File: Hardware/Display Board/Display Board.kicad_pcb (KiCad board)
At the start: 2 copper layers, 165.1 x 88.9 mm, 44 parts, among them J1 GPS, J10 Conn_02x03_Odd_Even, J11 Conn_02x03_Odd_Even, J12 Conn_02x03_Odd_Even, J13 Conn_02x03_Odd_Even, J14 Conn_02x03_Odd_Even, J15 Conn_02x03_Odd_Even, J16 Conn_02x03_Odd_Even, J17 Conn_02x03_Odd_Even, J18 Conn_02x03_Odd_Even, J19 Conn_02x03_Odd_Even, J2 RTC, J20 Conn_02x03_Odd_Even, J21 Conn_02x03_Odd_Even, J22 Conn_02x03_Odd_Even, J23 Conn_02x03_Odd_Even, J24 Conn_02x03_Odd_Even, J25 Conn_02x03_Odd_Even, J26 Conn_02x03_Odd_Even, J27 Conn_02x03_Odd_Even, J28 Conn_02x03_Odd_Even, J29 Conn_02x03_Odd_Even, J3 CONT, J30 Conn_02x03_Odd_Even, J31 Conn_02x03_Odd_Even, J4 H:M, J5 M:D, J6 M:S, J7 D:Y, J8 Conn_02x03_Odd_Even, J9 Conn_02x03_Odd_Even

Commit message: Components placed
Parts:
- J1, J2, J3: moved to B.Cu
- moved J21 282.3 mm to (77.5, 147.3), turned to -90 degrees
- moved J20 271.6 mm to (72.4, 119.4), turned to 90 degrees
- moved J9 266.6 mm to (77.5, 96.5), turned to -90 degrees
- moved J23 265.7 mm to (100.3, 147.3), turned to -90 degrees
- moved J8 262.1 mm to (72.4, 68.6), turned to 90 degrees
- moved J11 260.1 mm to (100.3, 96.5), turned to -90 degrees
- moved J10 255.5 mm to (95.2, 68.6), turned to 90 degrees
- moved J22 253.3 mm to (95.3, 119.4), turned to 90 degrees
- moved J25 250.2 mm to (130.8, 147.3), turned to -90 degrees
- moved J24 234.5 mm to (125.7, 119.4), turned to 90 degrees
- moved J13 222.8 mm to (130.8, 96.5), turned to -90 degrees
- moved J29 220.0 mm to (184.2, 147.3), turned to -90 degrees
- moved J12 213.3 mm to (125.7, 68.6), turned to 90 degrees
- moved J28 202.2 mm to (179.1, 119.4), turned to 90 degrees
- moved J27 189.6 mm to (153.7, 147.3), turned to -90 degrees
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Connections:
- J1 pad 2: unconnected-(J1-Pin_2-Pad2) -> MCU RX / GPS TX
- J1 pad 3: unconnected-(J1-Pin_3-Pad3) -> MCU TX / GPS RX
- J2 pad 3: unconnected-(J2-Pin_3-Pad3) -> SDA
- J2 pad 4: unconnected-(J2-Pin_4-Pad4) -> SCL
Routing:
- added copper zone on B.Cu, net GND

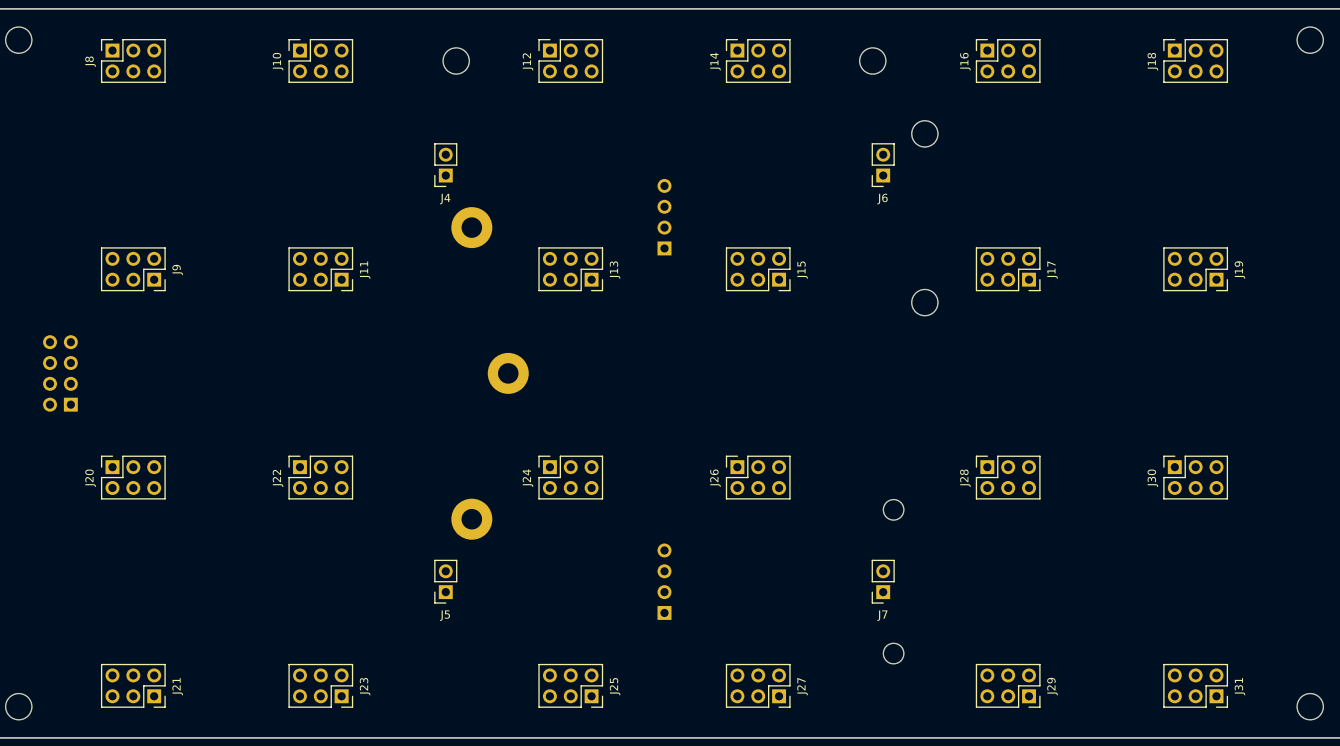
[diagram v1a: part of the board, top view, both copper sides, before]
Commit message: KiCad display board completed
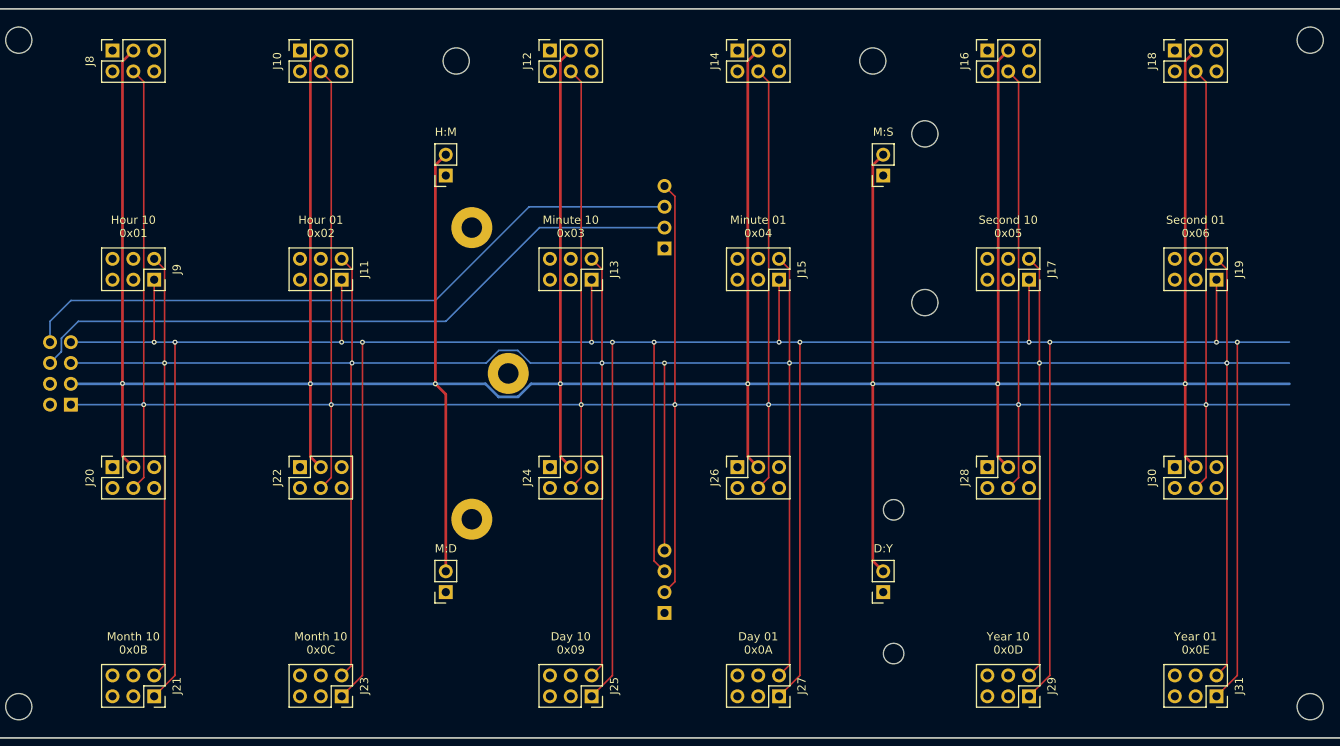
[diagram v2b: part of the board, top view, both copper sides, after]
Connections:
- J21 pad 5: GND -> /Month10/ADDR1
- J23 pad 4: GND -> /Month01/ADDR2
- J23 pad 5: /Month01/ADDR1 -> GND
- J25 pad 5: /Day10/ADDR1 -> GND
- J27 pad 4: /Day01/ADDR2 -> GND
- J27 pad 5: GND -> /Day01/ADDR1
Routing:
- net Vnn: track 0.00 -> 564.9 mm, vias 0 -> 8
- net Vdd: track 0.00 -> 510.3 mm, vias 0 -> 7
- net SDA: track 0.00 -> 488.2 mm, vias 0 -> 13
- net SCL: track 0.00 -> 483.8 mm, vias 0 -> 7
- net MCU TX / GPS RX: track 0.00 -> 83.3 mm
- net MCU RX / GPS TX: track 0.00 -> 82.7 mm
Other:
- board text added: "Day 01 0x0A"
- board text added: "Day 10 0x09"
- board text added: "Hour 01 0x02"
- board text added: "Hour 10 0x01"
- board text added: "Minute 01 0x04"
- board text added: "Minute 10 0x03"
- board text added: "Month 10 0x0B"
- board text added: "Month 10 0x0C"
- board text added: "Second 01 0x06"
- board text added: "Second 10 0x05"
- board text added: "Year 01 0x0E"
- board text added: "Year 10 0x0D"

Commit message: Forgot to save again. (╯°□°）╯︵ ┻━┻
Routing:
- net Vnn: track 564.9 -> 552.2 mm
- net Vdd: track 510.3 -> 500.1 mm
- net SCL: track 483.8 -> 476.2 mm
- net SDA: track 488.2 -> 481.8 mm
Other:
- board text added: "Month 01 0x0C"
- board text added: "Nixie Clock Aaron Johnson 12/17/2024"
- board text removed: "Month 10 0x0C"
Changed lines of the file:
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@@
 		)
 	)
-	(gr_text "Month 10\n0x0C"
+	(gr_text "Month 01\n0x0C"
 		(at 97.79 142.24 0)
 		(layer "F.SilkS")
@@
 			)
 			(justify bottom)
+		)
+	)
+	(gr_text "Nixie Clock\nAaron Johnson\n12/17/2024"
+		(at 220.98 107.95 -90)
+		(layer "F.SilkS")
+		(effects
+			(font
+				(size 1 1)
+				(thickness 0.1)
+			)
+			(justify top)
 		)
 	)
@@
 	)
 	(segment
-		(start 205.74 111.76)
-		(end 215.9 111.76)
-		(width 0.2)
-		(layer "B.Cu")
-		(net 2)
-	)
-	(segment
 		(start 99.06 111.76)
 		(end 129.54 111.76)
@@
 	)
 	(segment
-		(start 203.2 109.22)
-		(end 215.9 109.22)
-		(width 0.33)
-		(layer "B.Cu")
-		(net 3)
-	)
-	(segment
 		(start 127 109.22)
 		(end 149.86 109.22)
@@
 	)
 	(segment
-		(start 208.28 106.68)
-		(end 215.9 106.68)
-		(width 0.2)
-		(layer "B.Cu")
-		(net 5)
-	)
-	(segment
 		(start 119.490202 105.15)
 		(end 121.809798 105.15)
@@
 		(width 0.2)
 		(layer "B.Cu")
-		(net 8)
-	)
-	(segment
-		(start 209.55 104.14)
-		(end 215.9 104.14)
-		(width 0.2)
-		(layer "B.Cu")
